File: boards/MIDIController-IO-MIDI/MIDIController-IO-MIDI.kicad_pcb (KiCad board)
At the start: 2 copper layers, 160 x 100 mm, 44 parts, among them J1 MIDI In 1, J10 MIDICon, J2 MIDI In 2, J3 MIDI In 3, J4 MIDI In 4, J5 MIDI In Pedal, J6 MIDI Out 1, J7 MIDI Out 2, J8 MIDI Out 3, J9 MIDI Out 4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

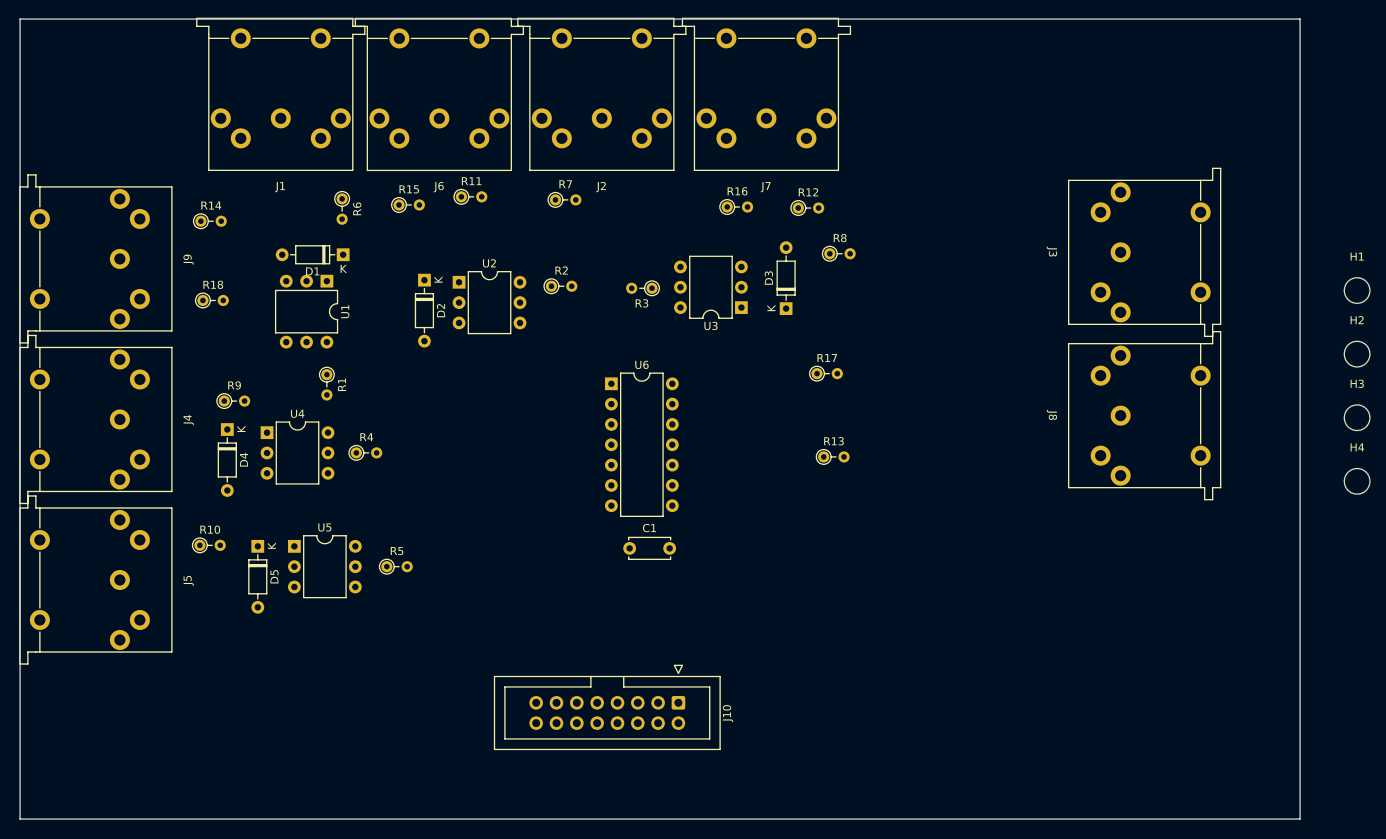
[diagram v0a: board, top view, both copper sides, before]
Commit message: Finished PCB for MIDI IO board
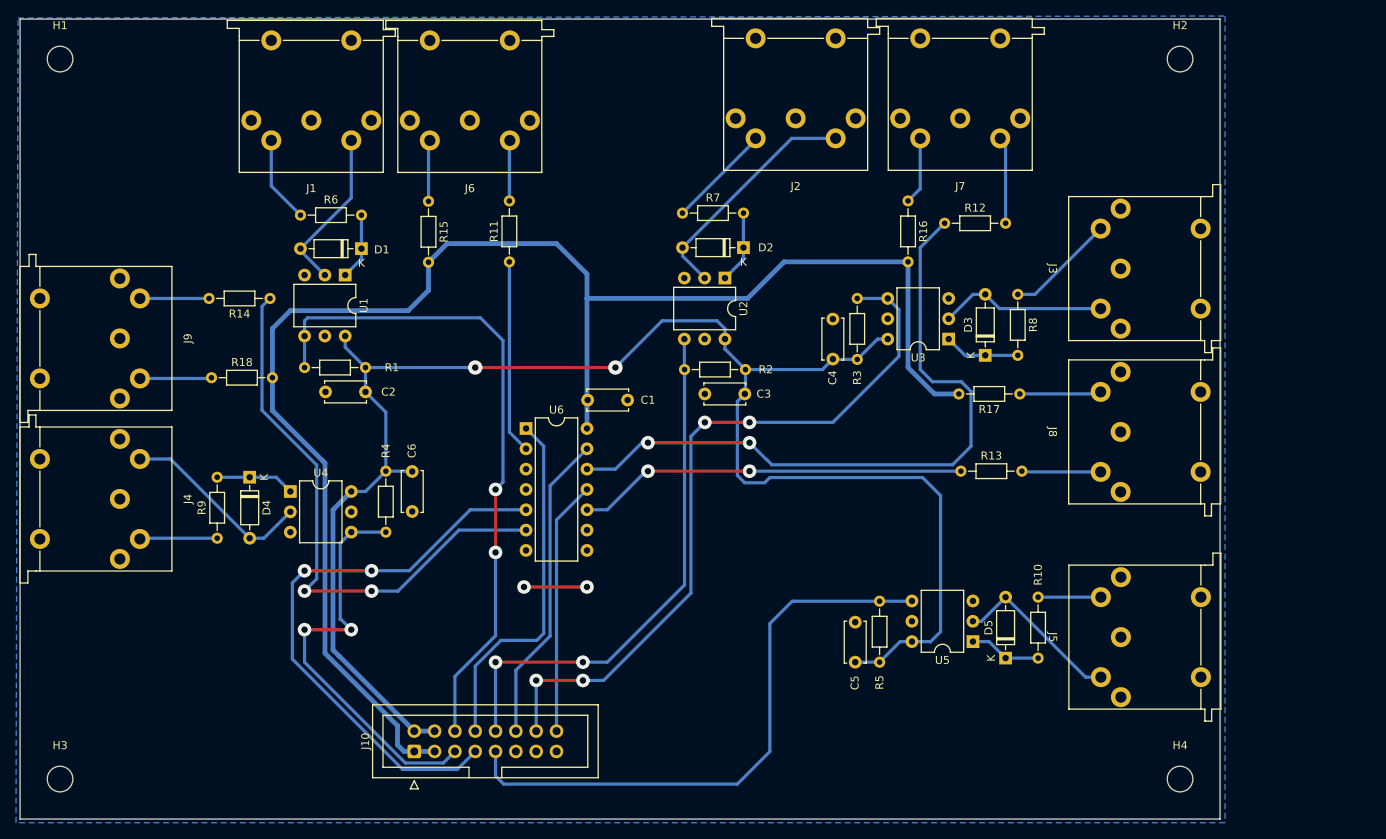
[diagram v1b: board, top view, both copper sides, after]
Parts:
- added C2: 100n, Capacitor_THT:C_Disc_D5.0mm_W2.5mm_P5.00mm, F.Cu at (110.7, 84.8)
- added C3: 100n, Capacitor_THT:C_Disc_D5.0mm_W2.5mm_P5.00mm, F.Cu at (158.2, 85.1)
- added C4: 100n, Capacitor_THT:C_Disc_D5.0mm_W2.5mm_P5.00mm, F.Cu at (169.2, 80.7)
- added C5: 100n, Capacitor_THT:C_Disc_D5.0mm_W2.5mm_P5.00mm, F.Cu at (172.0, 118.6)
- added C6: 100n, Capacitor_THT:C_Disc_D5.0mm_W2.5mm_P5.00mm, F.Cu at (116.6, 94.8)
- R1, R10, R11, R12, R13, R14, R15, R16, R17, R18, R2, R3, R4, R5, R6, R7, R8, R9: footprint Resistor_THT:R_Axial_DIN0204_L3.6mm_D1.6mm_P2.54mm_Vertical -> Resistor_THT:R_Axial_DIN0204_L3.6mm_D1.6mm_P7.62mm_Horizontal
- moved H3 168.3 mm to (72.6, 133.2)
- moved H1 164.7 mm to (72.6, 43.2)
- moved J5 125.3 mm to (205.2, 115.5), turned to -90 degrees
- moved R10 105.0 mm to (194.8, 110.5), turned to -90 degrees
- moved D5 94.5 mm to (190.8, 118.1), turned to 90 degrees
- moved U5 85.6 mm to (186.7, 116.0), turned to 180 degrees
- moved R5 62.7 mm to (175.0, 118.6), turned to 90 degrees
- moved H4 43.3 mm to (212.6, 133.2)
- moved H2 43.0 mm to (212.6, 43.2)
- moved D2 40.1 mm to (158.0, 66.8), turned to 180 degrees
- moved J10 33.6 mm to (116.8, 129.8), turned to 90 degrees
- moved U2 33.2 mm to (155.7, 70.6), turned to -90 degrees
- moved R3 27.2 mm to (172.2, 80.8), turned to 90 degrees
- moved R2 26.4 mm to (158.2, 82.0), turned to 180 degrees
- moved U3 26.2 mm to (183.6, 78.2)
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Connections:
- U6 pad 10: unconnected-(U6-Pad10) -> Net-(R13-Pad1)
- U6 pad 11: GND -> /MIDI_OUT3
- U6 pad 12: unconnected-(U6-Pad12) -> Net-(R12-Pad1)
- U6 pad 13: GND -> /MIDI_OUT2
- U6 pad 3: /MIDI_OUT2 -> GND
- U6 pad 4: Net-(R12-Pad1) -> unconnected-(U6-Pad4)
- U6 pad 5: /MIDI_OUT3 -> /MIDI_OUT4
- U6 pad 6: Net-(R13-Pad1) -> Net-(R14-Pad1)
- U6 pad 8: Net-(R14-Pad1) -> unconnected-(U6-Pad8)
- U6 pad 9: /MIDI_OUT4 -> GND
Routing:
- net +3.3V: track 0.00 -> 208.4 mm, vias 0 -> 2
- net +5V: track 0.00 -> 193.1 mm
- net /MIDI_IN3: track 0.00 -> 91.6 mm, vias 0 -> 4
- net Net-(R12-Pad1): track 0.00 -> 85.4 mm, vias 0 -> 2
- net /MIDI_IN1: track 0.00 -> 83.3 mm, vias 0 -> 2
- net /MIDI_IN_PED: track 0.00 -> 74.4 mm
- net /MIDI_OUT4: track 0.00 -> 72.0 mm, vias 0 -> 2
- net Net-(R14-Pad1): track 0.00 -> 71.3 mm, vias 0 -> 2
- net /MIDI_IN2: track 0.00 -> 67.0 mm, vias 0 -> 2
- net /MIDI_IN4: track 0.00 -> 52.3 mm, vias 0 -> 2
- net Net-(R13-Pad1): track 0.00 -> 48.7 mm, vias 0 -> 2
- net /MIDI_OUT1: track 0.00 -> 44.9 mm
- net /MIDI_OUT2: track 0.00 -> 39.0 mm
- net /MIDI_OUT3: track 0.00 -> 31.8 mm
- net Net-(D2-A): track 0.00 -> 29.8 mm
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- added copper zone on B.Cu, net GND
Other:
- board size 160 x 100 mm -> 150 x 100 mm

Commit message: Added Optocoupler and RS232 converter to UART board lines.
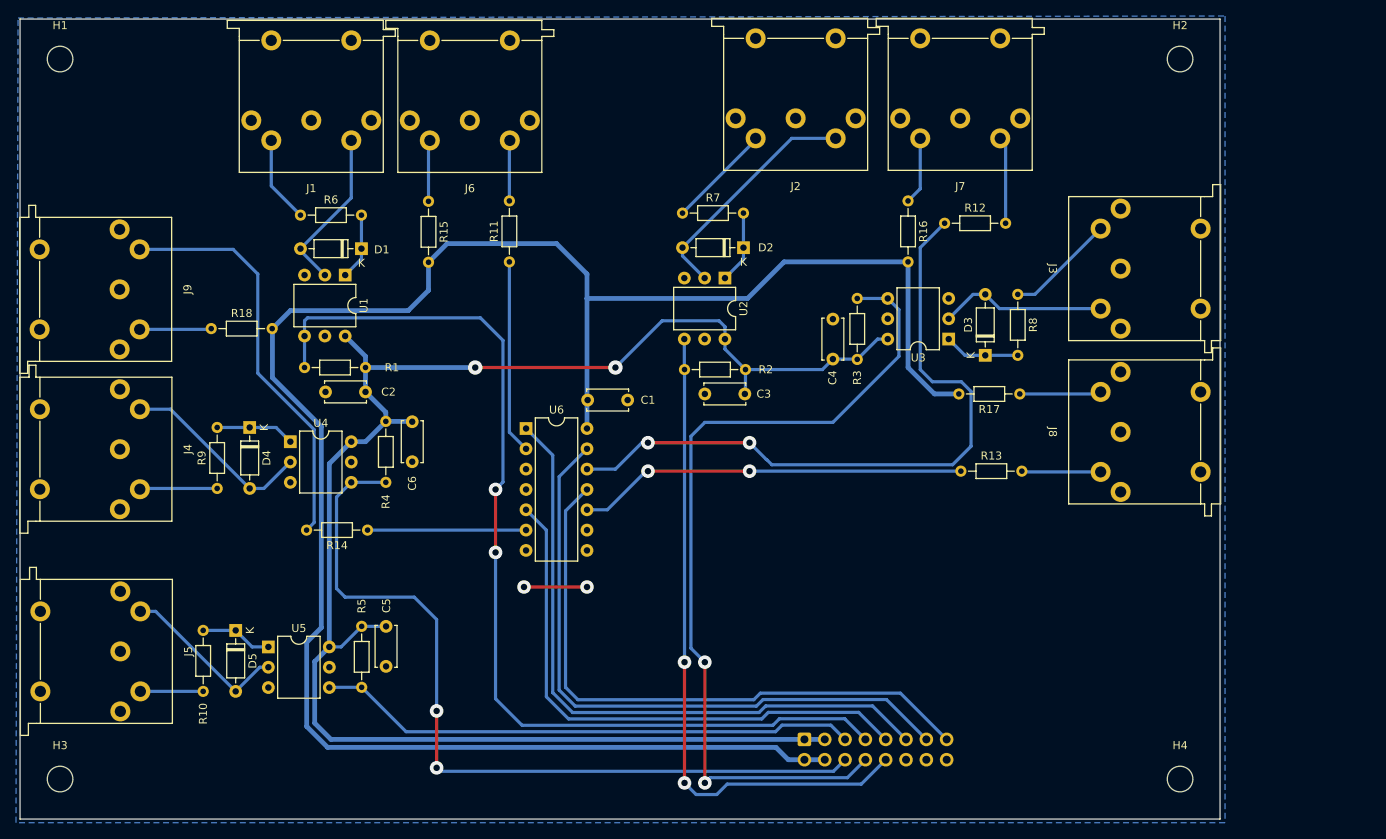
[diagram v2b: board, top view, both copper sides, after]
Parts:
- J1: value MIDI In 1 -> MIDI In 2
- J10: moved to B.Cu
- J2: value MIDI In 2 -> MIDI In 3
- J3: value MIDI In 3 -> MIDI In 4
- J4: value MIDI In 4 -> MIDI In 1
- J6: value MIDI Out 1 -> MIDI Out 2
- J7: value MIDI Out 2 -> MIDI Out 3
- J8: value MIDI Out 3 -> MIDI Out 4
- J9: value MIDI Out 4 -> MIDI Out 1
- moved J5 125.1 mm to (80.1, 117.3), turned to 90 degrees
- moved R10 105.0 mm to (90.5, 122.3), turned to 90 degrees
- moved D5 96.3 mm to (94.5, 114.6), turned to -90 degrees
- moved U5 88.1 mm to (98.6, 116.7), turned to 0 degrees
- moved R5 64.9 mm to (110.3, 114.1), turned to -90 degrees
- moved C5 58.8 mm to (113.3, 114.1), turned to -90 degrees
- moved J10 48.8 mm to (165.6, 128.3), turned to -90 degrees
- moved R14 31.4 mm to (111.0, 102.1)
- moved C6 6.22 mm to (116.6, 88.6)
- moved D4 6.22 mm to (96.3, 89.3)
- moved J4 6.22 mm to (80.0, 92.0)
- moved R4 6.22 mm to (113.3, 88.5)
- moved R9 6.22 mm to (92.2, 96.9)
- moved U4 6.22 mm to (101.3, 91.1)
- moved R18 6.14 mm to (91.5, 76.9)
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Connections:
- J10 pad 1: +5V -> +3.3V
- J10 pad 10: /MIDI_IN2 -> /MIDI_IN3
- J10 pad 11: GND -> /MIDI_OUT2
- J10 pad 12: /MIDI_OUT2 -> GND
- J10 pad 13: GND -> /MIDI_OUT3
- J10 pad 14: /MIDI_IN3 -> GND
- J10 pad 15: GND -> /MIDI_OUT4
- J10 pad 16: /MIDI_OUT3 -> GND
- J10 pad 2: +3.3V -> +5V
- J10 pad 3: +5V -> +3.3V
- J10 pad 4: +3.3V -> +5V
- J10 pad 5: /MIDI_IN4 -> /MIDI_IN_PED
- J10 pad 7: /MIDI_OUT4 -> /MIDI_IN2
- J10 pad 8: /MIDI_OUT1 -> /MIDI_IN4
- J10 pad 9: /MIDI_IN_PED -> /MIDI_OUT1
- R1 pad 2: /MIDI_IN1 -> /MIDI_IN2
- R2 pad 2: /MIDI_IN2 -> /MIDI_IN3
- R3 pad 2: /MIDI_IN3 -> /MIDI_IN4
- R4 pad 2: /MIDI_IN4 -> /MIDI_IN1
- U1 pad 4: /MIDI_IN1 -> /MIDI_IN2
- U2 pad 4: /MIDI_IN2 -> /MIDI_IN3
- U3 pad 4: /MIDI_IN3 -> /MIDI_IN4
- U4 pad 4: /MIDI_IN4 -> /MIDI_IN1
- U6 pad 1: /MIDI_OUT1 -> /MIDI_OUT2
- U6 pad 11: /MIDI_OUT3 -> /MIDI_OUT4
- U6 pad 13: /MIDI_OUT2 -> /MIDI_OUT3
- U6 pad 5: /MIDI_OUT4 -> /MIDI_OUT1
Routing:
- net /MIDI_IN2: track 67.0 -> 126.2 mm
- net +5V: track 193.1 -> 249.1 mm
- net /MIDI_IN4: track 52.3 -> 107.1 mm
- net Net-(R14-Pad1): track 71.3 -> 19.8 mm, vias 2 -> 0
- net /MIDI_OUT3: track 31.8 -> 80.7 mm
- net Net-(J9-Pad5): track 8.54 -> 51.4 mm
- net /MIDI_OUT2: track 39.0 -> 81.7 mm
- net /MIDI_OUT1: track 44.9 -> 69.7 mm
- net /MIDI_IN1: track 83.3 -> 102.8 mm
- net /MIDI_IN3: track 91.6 -> 83.0 mm, vias 4 -> 2
- net /MIDI_IN_PED: track 74.4 -> 67.8 mm
- net /MIDI_OUT4: track 72.0 -> 76.9 mm, vias 2 -> 0
- net +3.3V: track 208.4 -> 207.6 mm

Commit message: Added bypass caps to power supplies, use cheaper MAX232 IC.
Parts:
- J10: moved to F.Cu
- moved J10 17.8 mm to (183.4, 128.0)
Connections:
- J10 pad 1: +3.3V -> /MIDI_OUT4
- J10 pad 10: /MIDI_IN3 -> /MIDI_IN4
- J10 pad 11: /MIDI_OUT2 -> /MIDI_IN_PED
- J10 pad 12: GND -> /MIDI_IN1
- J10 pad 13: /MIDI_OUT3 -> +3.3V
- J10 pad 14: GND -> +5V
- J10 pad 15: /MIDI_OUT4 -> +3.3V
- J10 pad 16: GND -> +5V
- J10 pad 2: +5V -> GND
- J10 pad 3: +3.3V -> /MIDI_OUT3
- J10 pad 4: +5V -> GND
- J10 pad 5: /MIDI_IN_PED -> /MIDI_OUT2
- J10 pad 6: /MIDI_IN1 -> GND
- J10 pad 7: /MIDI_IN2 -> /MIDI_OUT1
- J10 pad 8: /MIDI_IN4 -> /MIDI_IN3
- J10 pad 9: /MIDI_OUT1 -> /MIDI_IN2

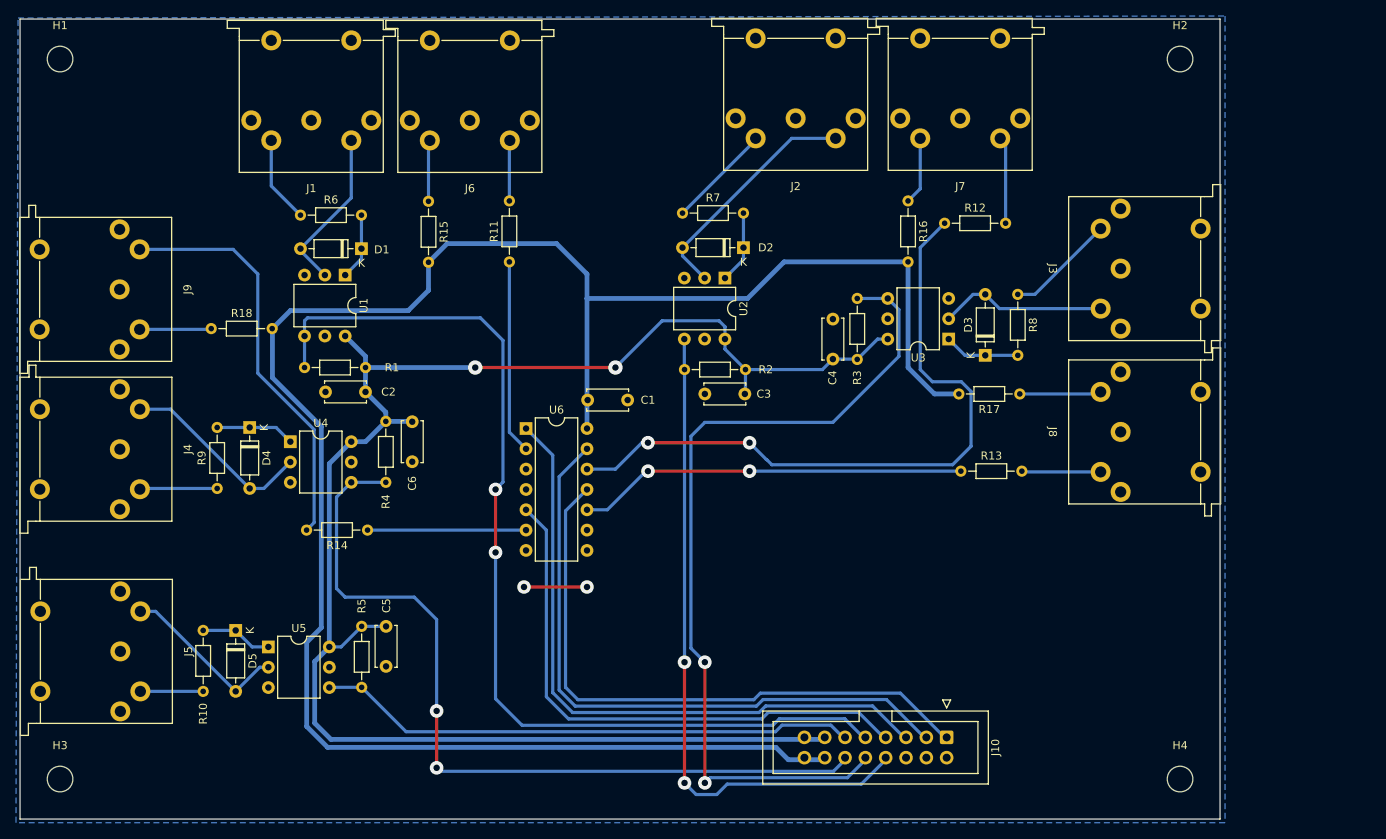
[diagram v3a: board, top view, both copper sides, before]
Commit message: Updated design rules to 0.32mm template and exported Gerber files
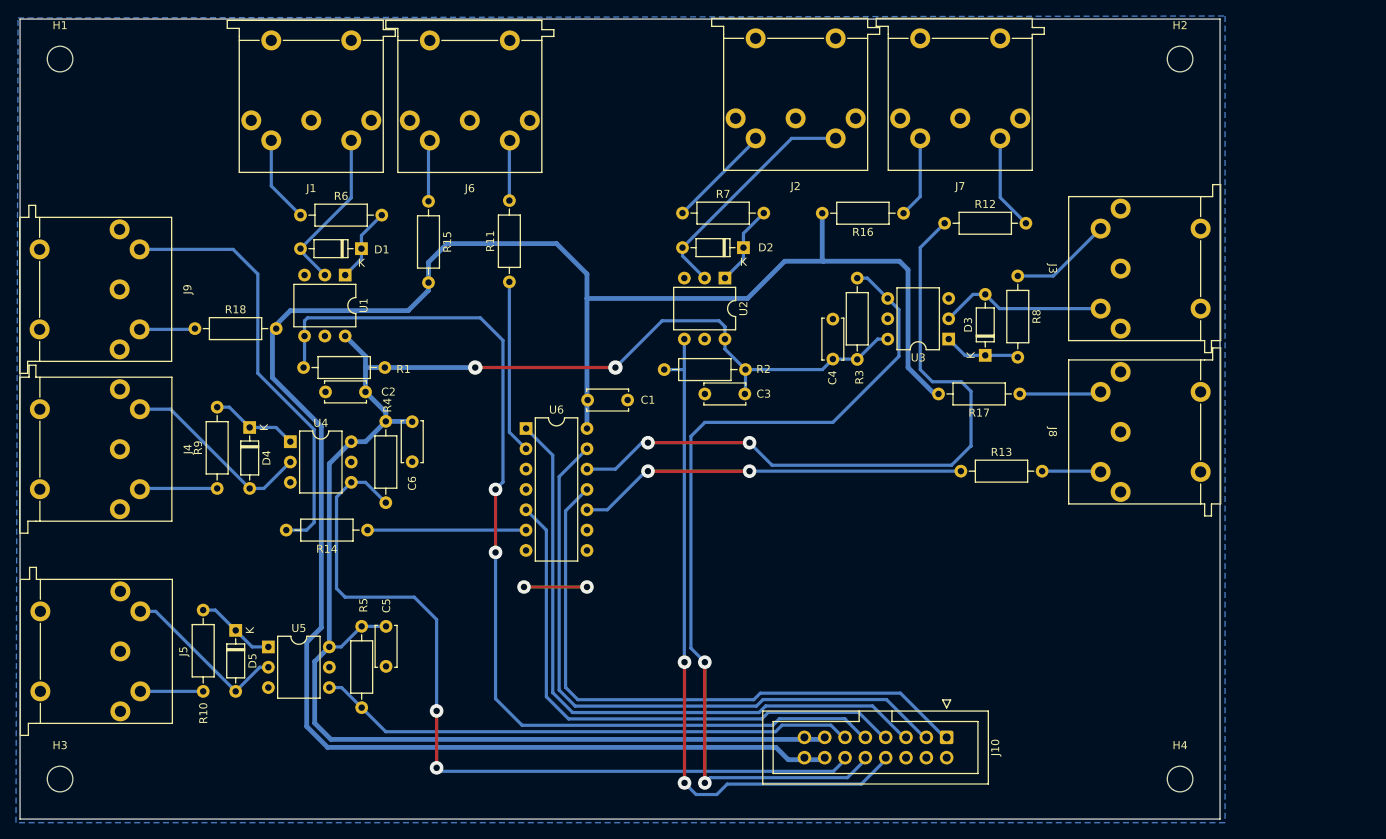
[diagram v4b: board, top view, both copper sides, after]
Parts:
- R1, R10, R11, R12, R13, R14, R15, R16, R17, R18, R2, R3, R4, R5, R6, R7, R8, R9: footprint Resistor_THT:R_Axial_DIN0204_L3.6mm_D1.6mm_P7.62mm_Horizontal -> Resistor_THT:R_Axial_DIN0207_L6.3mm_D2.5mm_P10.16mm_Horizontal
- moved R11 2.50 mm to (128.7, 71.1)
- moved R1 2.42 mm to (113.2, 81.8)
- moved R8 2.30 mm to (192.3, 70.3)
- moved R18 2.04 mm to (89.4, 76.9)
- moved R16 1.64 mm to (178.0, 62.5), turned to 180 degrees
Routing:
- net +5V: track 249.1 -> 252.1 mm
- net /MIDI_IN3: track 83.0 -> 85.6 mm
- net Net-(J9-Pad5): track 51.4 -> 53.9 mm
- net Net-(R11-Pad1): track 24.2 -> 21.7 mm
- net Net-(J8-Pad5): track 9.76 -> 7.35 mm
- net Net-(J7-Pad5): track 9.95 -> 11.9 mm
- net Net-(J9-Pad4): track 8.85 -> 6.95 mm
- net Net-(J7-Pad4): track 8.45 -> 10.2 mm
- net Net-(D4-K): track 9.88 -> 10.9 mm
- net /MIDI_IN4: track 107.1 -> 108.1 mm
- net /MIDI_IN1: track 102.8 -> 103.9 mm
- net Net-(D2-K): track 9.08 -> 10.1 mm
- net Net-(D5-K): track 9.00 -> 10.1 mm
- net Net-(D1-K): track 8.33 -> 9.39 mm
- net Net-(J3-Pad4): track 13.8 -> 12.8 mm
